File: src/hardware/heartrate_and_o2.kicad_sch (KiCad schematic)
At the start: 5 parts

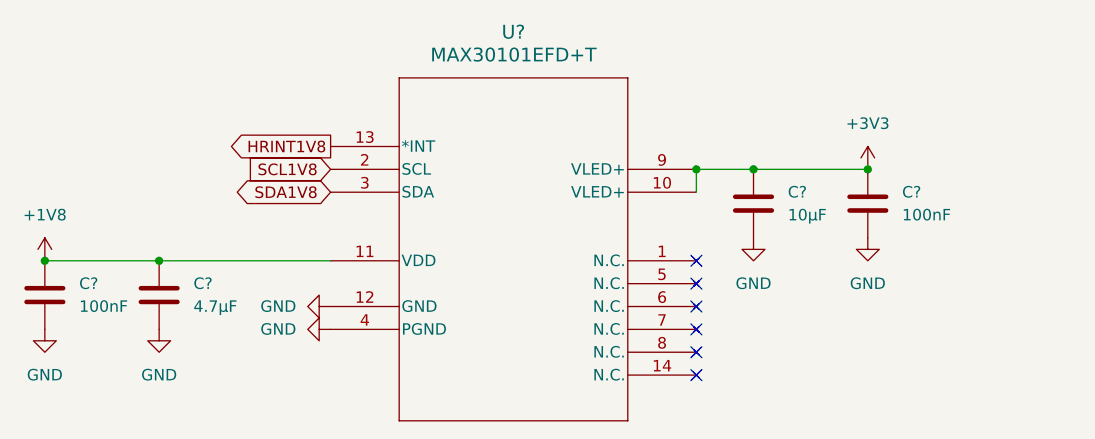
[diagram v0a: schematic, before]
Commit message: Added I²C Addresses
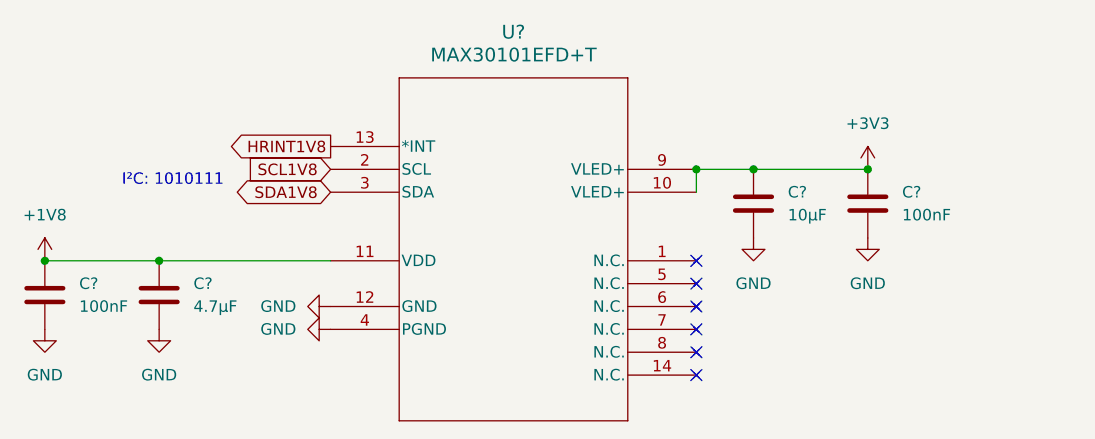
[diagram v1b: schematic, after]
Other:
- note added: "I²C: 1010111"
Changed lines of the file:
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@@
 		(date "2026-10-21")
+	)
+	(text "I²C: 1010111"
+		(exclude_from_sim no)
+		(at 108.204 91.44 0)
+		(effects
+			(font
+				(size 1.27 1.27)
+			)
+		)
 	)
 	(junction
@@
 			)
 		)
-		(property "Datasheet" "MAX30101EFD+T"
+		(property "Datasheet" "https://www.analog.com/media/en/technical-documentation/data-sheets/MAX30101.pdf"
 			(at 125.73 87.63 0)
 			(effects

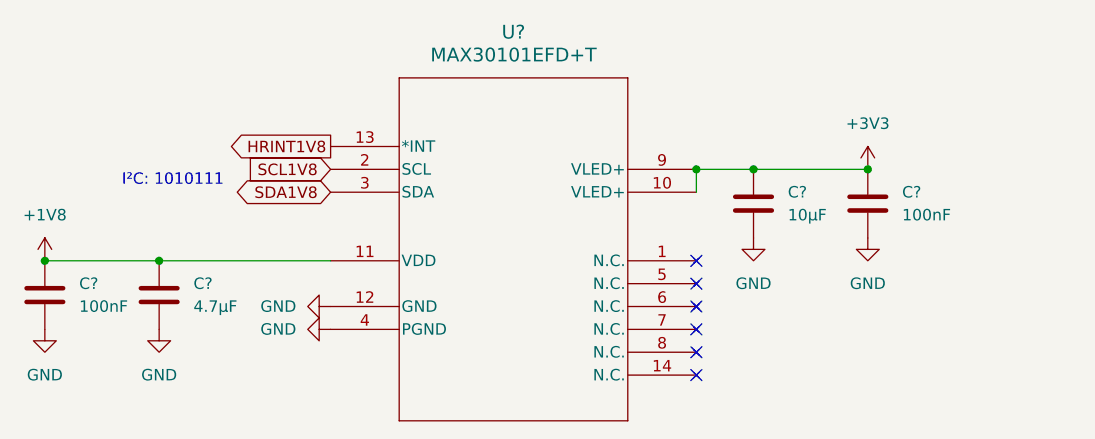
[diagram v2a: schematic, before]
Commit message: Replaced schematics, 3d models and footprints. Added vibration motor.
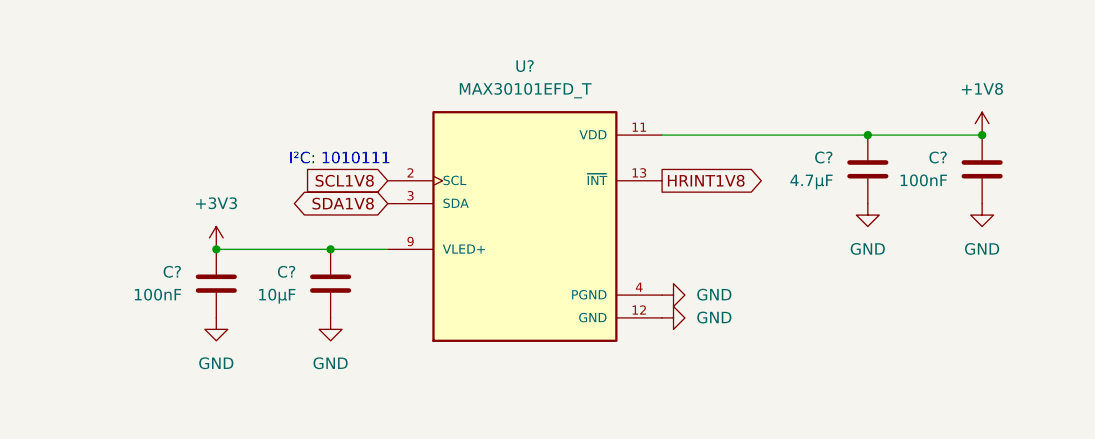
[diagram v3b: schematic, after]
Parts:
- removed U?: MAX30101EFD+T, 21-1048F_F143A5+1_MXM, symbol MAX30101EFD+T:MAX30101EFD+T
- added U?: MAX30101EFD_T, MAX30101EFD_T:PSON80P560X330X165-14N, symbol MAX30101EFD_T:MAX30101EFD_T
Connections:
- net +1V8: now also U?.11 (VDD)
- net +3V3: now also U?.10 (VLED+), U?.9 (VLED+)
- net GND: now also U?.12 (GND), U?.4 (PGND)
- net HRINT1V8: now also U?.13 (~{INT})
- net SCL1V8: now also U?.2 (SCL)
- net SDA1V8: now also U?.3 (SDA)
- no-connect marks 6 -> 0
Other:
- moved on the sheet: C?

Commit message: Added LoRa
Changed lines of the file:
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@@
 		(on_board yes)
 		(dnp no)
+		(fields_autoplaced yes)
 		(property "Reference" "C?"
 			(at 109.22 101.5999 0)
@@
 		(fields_autoplaced yes)
 		(property "Reference" "C?"
-			(at 194.31 88.8999 0)
-			(effects
-				(font
-					(size 1.27 1.27)
-				)
-				(justify left)
+			(at 201.93 88.8999 0)
+			(effects
+				(font
+					(size 1.27 1.27)
+				)
+				(justify right)
 			)
 		)
 		(property "Value" "100nF"
-			(at 194.31 91.4399 0)
-			(effects
-				(font
-					(size 1.27 1.27)
-				)
-				(justify left)
+			(at 201.93 91.4399 0)
+			(effects
+				(font
+					(size 1.27 1.27)
+				)
+				(justify right)
 			)
 		)
@@
 		(fields_autoplaced yes)
 		(property "Reference" "C?"
-			(at 181.61 88.8999 0)
-			(effects
-				(font
-					(size 1.27 1.27)
-				)
-				(justify left)
+			(at 189.23 88.8999 0)
+			(effects
+				(font
+					(size 1.27 1.27)
+				)
+				(justify right)
 			)
 		)
 		(property "Value" "4.7µF"
-			(at 181.61 91.4399 0)
-			(effects
-				(font
-					(size 1.27 1.27)
-				)
-				(justify left)
-			)
-		)
+			(at 189.23 91.4399 0)
+			(effects
+				(font
+					(size 1.27 1.27)
+				)
+				(justify right)
+			)
+		)

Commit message: Changed 5V net to 4.5V net
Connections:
- net +3V3 renamed +4V5
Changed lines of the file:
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@@
 			)
 		)
-		(property "Value" "+3V3"
-			(at 113.03 93.98 0)
+		(property "Value" "+4V5"
+			(at 115.57 97.7899 0)
 			(effects
 				(font
 					(size 1.27 1.27)
 				)
+				(justify right)
 			)
 		)

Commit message: Cleanup & Fixes; Added footprints; Removed Light sensors
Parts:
- C49, C50, C51, C52: renamed from C?; footprint (none) -> Capacitor_SMD:C_0603_1608Metric
- U16: renamed from U?; footprint MAX30101EFD_T:PSON80P560X330X165-14N -> Project:PSON80P560X330X165-14N
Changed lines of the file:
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@@
 		(dnp no)
 		(fields_autoplaced yes)
-		(property "Reference" "C?"
+		(property "Reference" "C49"
 			(at 109.22 101.5999 0)
 			(effects
@@
 			)
 		)
-		(property "Footprint" ""
+		(property "Footprint" "Capacitor_SMD:C_0603_1608Metric"
 			(at 112.0648 106.68 0)
 			(effects
@@
 			(project "raywatch"
 				(path "/7b654ee8-2a53-4d39-8b7d-32c7bb3cb0ed/92973ecd-838d-4692-844f-05a1efeb365a"
-					(reference "C?")
+					(reference "C49")
 					(unit 1)
 				)
@@
 		(dnp no)
 		(fields_autoplaced yes)
-		(property "Reference" "#PWR0298"
+		(property "Reference" "#PWR0307"
 			(at 198.12 90.17 0)
 			(effects
@@
 			(project "raywatch"
 				(path "/7b654ee8-2a53-4d39-8b7d-32c7bb3cb0ed/92973ecd-838d-4692-844f-05a1efeb365a"
-					(reference "#PWR0298")
+					(reference "#PWR0307")
 					(unit 1)
 				)
@@
 		(dnp no)
 		(fields_autoplaced yes)
-		(property "Reference" "#PWR0295"
+		(property "Reference" "#PWR0303"
 			(at 125.73 113.03 0)
 			(effects
@@
 			(project "raywatch"
 				(path "/7b654ee8-2a53-4d39-8b7d-32c7bb3cb0ed/92973ecd-838d-4692-844f-05a1efeb365a"
-					(reference "#PWR0295")
+					(reference "#PWR0303")
 					(unit 1)
 				)
@@
 		(dnp no)
 		(fields_autoplaced yes)
-		(property "Reference" "#PWR0300"
+		(property "Reference" "#PWR0306"
 			(at 185.42 100.33 0)
 			(effects
@@
 			(project "raywatch"
 				(path "/7b654ee8-2a53-4d39-8b7d-32c7bb3cb0ed/92973ecd-838d-4692-844f-05a1efeb365a"
-					(reference "#PWR0300")
+					(reference "#PWR0306")
 					(unit 1)
 				)
@@
 		(dnp no)
 		(fields_autoplaced yes)
-		(property "Reference" "#PWR0297"
+		(property "Reference" "#PWR0301"
 			(at 113.03 102.87 0)
 			(effects
@@
 		)
 		(property "Value" "+4V5"
-			(at 115.57 97.7899 0)
-			(effects
-				(font
-					(size 1.27 1.27)
-				)
-				(justify right)
+			(at 113.03 93.98 0)
+			(effects
+				(font
+					(size 1.27 1.27)
+				)
 			)
 		)
@@
 			(project "raywatch"
 				(path "/7b654ee8-2a53-4d39-8b7d-32c7bb3cb0ed/92973ecd-838d-4692-844f-05a1efeb365a"
-					(reference "#PWR0297")
+					(reference "#PWR0301")
 					(unit 1)
 				)
@@
 		(dnp no)
 		(fields_autoplaced yes)
-		(property "Reference" "C?"
+		(property "Reference" "C52"
 			(at 201.93 88.8999 0)
 			(effects
@@
 			)
 		)
-		(property "Footprint" ""
+		(property "Footprint" "Capacitor_SMD:C_0603_1608Metric"
 			(at 197.1548 93.98 0)
 			(effects
@@
 			(project "raywatch"
 				(path "/7b654ee8-2a53-4d39-8b7d-32c7bb3cb0ed/92973ecd-838d-4692-844f-05a1efeb365a"
-					(reference "C?")
+					(reference "C52")
 					(unit 1)
 				)
@@
 		(dnp no)
 		(fields_autoplaced yes)
-		(property "Reference" "C?"
+		(property "Reference" "C50"
 			(at 121.92 101.5999 0)
 			(effects
@@
 			)
 		)
-		(property "Footprint" ""
+		(property "Footprint" "Capacitor_SMD:C_0603_1608Metric"
 			(at 124.7648 106.68 0)
 			(effects
@@
 			(project "raywatch"
 				(path "/7b654ee8-2a53-4d39-8b7d-32c7bb3cb0ed/92973ecd-838d-4692-844f-05a1efeb365a"
-					(reference "C?")
+					(reference "C50")
 					(unit 1)
 				)
@@
 		(dnp no)
 		(fields_autoplaced yes)
-		(property "Reference" "#PWR0294"
+		(property "Reference" "#PWR0304"
 			(at 168.91 104.14 0)
 			(effects
@@
 			(project "raywatch"
 				(path "/7b654ee8-2a53-4d39-8b7d-32c7bb3cb0ed/92973ecd-838d-4692-844f-05a1efeb365a"
-					(reference "#PWR0294")
+					(reference "#PWR0304")
 					(unit 1)
 				)
@@
 		(dnp no)
 		(fields_autoplaced yes)
-		(property "Reference" "U?"
+		(property "Reference" "U16"
 			(at 147.32 78.74 0)
 			(effects
@@
 			)
 		)
-		(property "Footprint" "MAX30101EFD_T:PSON80P560X330X165-14N"
+		(property "Footprint" "Project:PSON80P560X330X165-14N"
 			(at 147.32 96.52 0)
 			(effects
@@
 			(project "raywatch"
 				(path "/7b654ee8-2a53-4d39-8b7d-32c7bb3cb0ed/92973ecd-838d-4692-844f-05a1efeb365a"
-					(reference "U?")
+					(reference "U16")
 					(unit 1)
 				)
@@
 		(dnp no)
 		(fields_autoplaced yes)
-		(property "Reference" "#PWR0299"
+		(property "Reference" "#PWR0308"
 			(at 198.12 100.33 0)
 			(effects
@@
 			(project "raywatch"
 				(path "/7b654ee8-2a53-4d39-8b7d-32c7bb3cb0ed/92973ecd-838d-4692-844f-05a1efeb365a"
-					(reference "#PWR0299")
+					(reference "#PWR0308")
 					(unit 1)
 				)
@@
 		(dnp no)
 		(fields_autoplaced yes)
-		(property "Reference" "C?"
+		(property "Reference" "C51"
 			(at 189.23 88.8999 0)
 			(effects
@@
 			)
 		)
-		(property "Footprint" ""
+		(property "Footprint" "Capacitor_SMD:C_0603_1608Metric"
 			(at 184.4548 93.98 0)
 			(effects
@@
 			(project "raywatch"
 				(path "/7b654ee8-2a53-4d39-8b7d-32c7bb3cb0ed/92973ecd-838d-4692-844f-05a1efeb365a"
-					(reference "C?")
+					(reference "C51")
 					(unit 1)
 				)
@@
 		(dnp no)
 		(fields_autoplaced yes)
-		(property "Reference" "#PWR0293"
+		(property "Reference" "#PWR0305"
 			(at 168.91 106.68 0)
 			(effects
@@
 			(project "raywatch"
 				(path "/7b654ee8-2a53-4d39-8b7d-32c7bb3cb0ed/92973ecd-838d-4692-844f-05a1efeb365a"
-					(reference "#PWR0293")
+					(reference "#PWR0305")
 					(unit 1)
 				)
@@
 		(dnp no)
 		(fields_autoplaced yes)
-		(property "Reference" "#PWR0296"
+		(property "Reference" "#PWR0302"
 			(at 113.03 113.03 0)
 			(effects
@@
 			(project "raywatch"
 				(path "/7b654ee8-2a53-4d39-8b7d-32c7bb3cb0ed/92973ecd-838d-4692-844f-05a1efeb365a"
-					(reference "#PWR0296")
-					(unit 1)
-				)
+					(reference "#PWR0302")
+					(unit 1)
+				)

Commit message: Cleanup & Fixes; Changed GPIO; Added Camera; Added Microphone
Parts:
- renumbered C49 to C47, C50 to C48, C51 to C49, C52 to C50
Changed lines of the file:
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@@
 		(dnp no)
 		(fields_autoplaced yes)
-		(property "Reference" "C49"
+		(property "Reference" "C47"
 			(at 109.22 101.5999 0)
 			(effects
@@
 			(project "raywatch"
 				(path "/7b654ee8-2a53-4d39-8b7d-32c7bb3cb0ed/92973ecd-838d-4692-844f-05a1efeb365a"
-					(reference "C49")
+					(reference "C47")
 					(unit 1)
 				)
@@
 		(dnp no)
 		(fields_autoplaced yes)
-		(property "Reference" "#PWR0307"
+		(property "Reference" "#PWR0303"
 			(at 198.12 90.17 0)
 			(effects
@@
 			(project "raywatch"
 				(path "/7b654ee8-2a53-4d39-8b7d-32c7bb3cb0ed/92973ecd-838d-4692-844f-05a1efeb365a"
-					(reference "#PWR0307")
+					(reference "#PWR0303")
 					(unit 1)
 				)
@@
 		(dnp no)
 		(fields_autoplaced yes)
-		(property "Reference" "#PWR0303"
+		(property "Reference" "#PWR0299"
 			(at 125.73 113.03 0)
 			(effects
@@
 			(project "raywatch"
 				(path "/7b654ee8-2a53-4d39-8b7d-32c7bb3cb0ed/92973ecd-838d-4692-844f-05a1efeb365a"
-					(reference "#PWR0303")
+					(reference "#PWR0299")
 					(unit 1)
 				)
@@
 		(dnp no)
 		(fields_autoplaced yes)
-		(property "Reference" "#PWR0306"
+		(property "Reference" "#PWR0302"
 			(at 185.42 100.33 0)
 			(effects
@@
 			(project "raywatch"
 				(path "/7b654ee8-2a53-4d39-8b7d-32c7bb3cb0ed/92973ecd-838d-4692-844f-05a1efeb365a"
-					(reference "#PWR0306")
+					(reference "#PWR0302")
 					(unit 1)
 				)
@@
 		(dnp no)
 		(fields_autoplaced yes)
-		(property "Reference" "#PWR0301"
+		(property "Reference" "#PWR0297"
 			(at 113.03 102.87 0)
 			(effects
@@
 			(project "raywatch"
 				(path "/7b654ee8-2a53-4d39-8b7d-32c7bb3cb0ed/92973ecd-838d-4692-844f-05a1efeb365a"
-					(reference "#PWR0301")
+					(reference "#PWR0297")
 					(unit 1)
 				)
@@
 		(dnp no)
 		(fields_autoplaced yes)
-		(property "Reference" "C52"
+		(property "Reference" "C50"
 			(at 201.93 88.8999 0)
 			(effects
@@
 			(project "raywatch"
 				(path "/7b654ee8-2a53-4d39-8b7d-32c7bb3cb0ed/92973ecd-838d-4692-844f-05a1efeb365a"
-					(reference "C52")
+					(reference "C50")
 					(unit 1)
 				)
@@
 		(dnp no)
 		(fields_autoplaced yes)
-		(property "Reference" "C50"
+		(property "Reference" "C48"
 			(at 121.92 101.5999 0)
 			(effects
@@
 			(project "raywatch"
 				(path "/7b654ee8-2a53-4d39-8b7d-32c7bb3cb0ed/92973ecd-838d-4692-844f-05a1efeb365a"
-					(reference "C50")
+					(reference "C48")
 					(unit 1)
 				)
@@
 		(dnp no)
 		(fields_autoplaced yes)
-		(property "Reference" "#PWR0304"
+		(property "Reference" "#PWR0300"
 			(at 168.91 104.14 0)
 			(effects
@@
 			(project "raywatch"
 				(path "/7b654ee8-2a53-4d39-8b7d-32c7bb3cb0ed/92973ecd-838d-4692-844f-05a1efeb365a"
-					(reference "#PWR0304")
+					(reference "#PWR0300")
 					(unit 1)
 				)
@@
 		(dnp no)
 		(fields_autoplaced yes)
-		(property "Reference" "#PWR0308"
+		(property "Reference" "#PWR0304"
 			(at 198.12 100.33 0)
 			(effects
@@
 			(project "raywatch"
 				(path "/7b654ee8-2a53-4d39-8b7d-32c7bb3cb0ed/92973ecd-838d-4692-844f-05a1efeb365a"
-					(reference "#PWR0308")
+					(reference "#PWR0304")
 					(unit 1)
 				)
@@
 		(dnp no)
 		(fields_autoplaced yes)
-		(property "Reference" "C51"
+		(property "Reference" "C49"
 			(at 189.23 88.8999 0)
 			(effects
@@
 			(project "raywatch"
 				(path "/7b654ee8-2a53-4d39-8b7d-32c7bb3cb0ed/92973ecd-838d-4692-844f-05a1efeb365a"
-					(reference "C51")
+					(reference "C49")
 					(unit 1)
 				)
@@
 		(dnp no)
 		(fields_autoplaced yes)
-		(property "Reference" "#PWR0305"
+		(property "Reference" "#PWR0301"
 			(at 168.91 106.68 0)
 			(effects
@@
 			(project "raywatch"
 				(path "/7b654ee8-2a53-4d39-8b7d-32c7bb3cb0ed/92973ecd-838d-4692-844f-05a1efeb365a"
-					(reference "#PWR0305")
+					(reference "#PWR0301")
 					(unit 1)
 				)
@@
 		(dnp no)
 		(fields_autoplaced yes)
-		(property "Reference" "#PWR0302"
+		(property "Reference" "#PWR0298"
 			(at 113.03 113.03 0)
 			(effects
@@
 			(project "raywatch"
 				(path "/7b654ee8-2a53-4d39-8b7d-32c7bb3cb0ed/92973ecd-838d-4692-844f-05a1efeb365a"
-					(reference "#PWR0302")
-					(unit 1)
-				)
+					(reference "#PWR0298")
+					(unit 1)
+				)
